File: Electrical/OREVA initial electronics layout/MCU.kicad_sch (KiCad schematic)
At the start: 1 part, among them J1 Raspberry_Pi_2_3

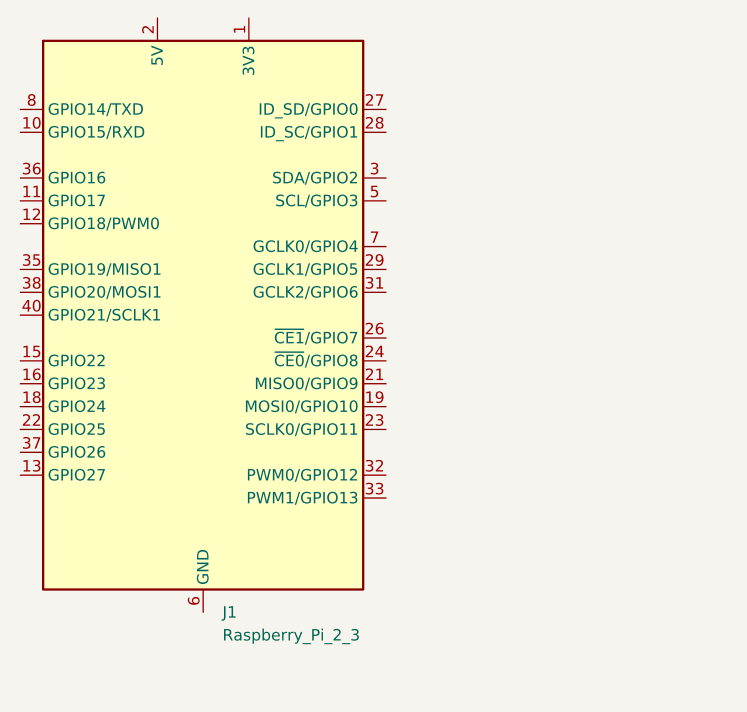
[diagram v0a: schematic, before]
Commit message: Added the MCU block pinout
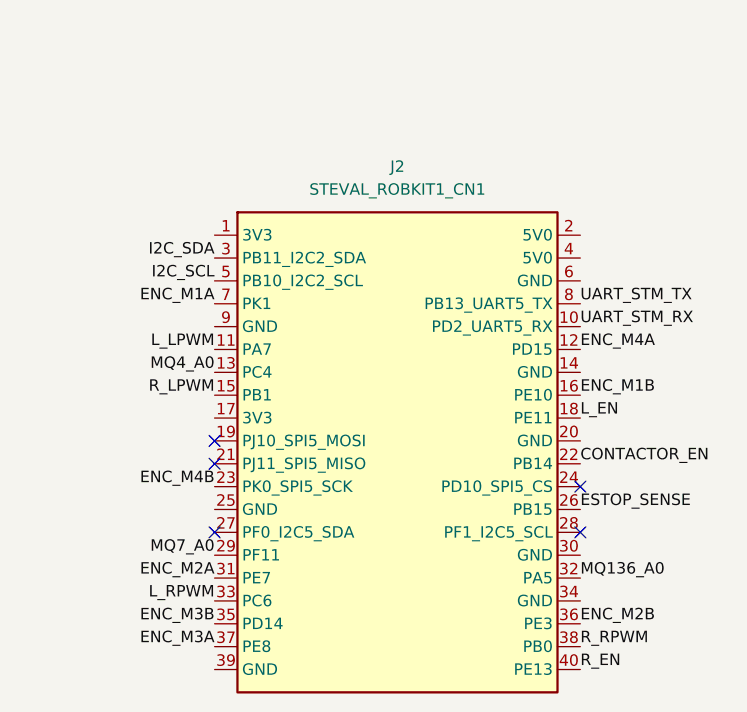
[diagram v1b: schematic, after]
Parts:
- removed J1: Raspberry_Pi_2_3, symbol Connector:Raspberry_Pi_2_3
- added J2: STEVAL_ROBKIT1_CN1, symbol OREVA_Custom:STEVAL_ROBKIT1_CN1
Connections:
- new net CONTACTOR_EN: J2.22 (PB14)
- new net ENC_M1A: J2.7 (PK1)
- new net ENC_M1B: J2.16 (PE10)
- new net ENC_M2A: J2.31 (PE7)
- new net ENC_M2B: J2.36 (PE3)
- new net ENC_M3A: J2.37 (PE8)
- new net ENC_M3B: J2.35 (PD14)
- new net ENC_M4A: J2.12 (PD15)
- new net ENC_M4B: J2.23 (PK0_SPI5_SCK)
- new net ESTOP_SENSE: J2.26 (PB15)
- new net I2C_SCL: J2.5 (PB10_I2C2_SCL)
- new net I2C_SDA: J2.3 (PB11_I2C2_SDA)
- new net L_EN: J2.18 (PE11)
- new net L_LPWM: J2.11 (PA7)
- new net L_RPWM: J2.33 (PC6)
- new net MQ136_A0: J2.32 (PA5)
- new net MQ4_A0: J2.13 (PC4)
- new net MQ7_A0: J2.29 (PF11)
- new net R_EN: J2.40 (PE13)
- new net R_LPWM: J2.15 (PB1)
- new net R_RPWM: J2.38 (PB0)
- new net UART_STM_RX: J2.10 (PD2_UART5_RX)
- new net UART_STM_TX: J2.8 (PB13_UART5_TX)
- no-connect marks 0 -> 5
